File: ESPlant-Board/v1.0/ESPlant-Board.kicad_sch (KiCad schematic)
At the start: 24 parts, among them J2 Programmer, Q1 NPN, Q2 NPN, U1 ESP-12F

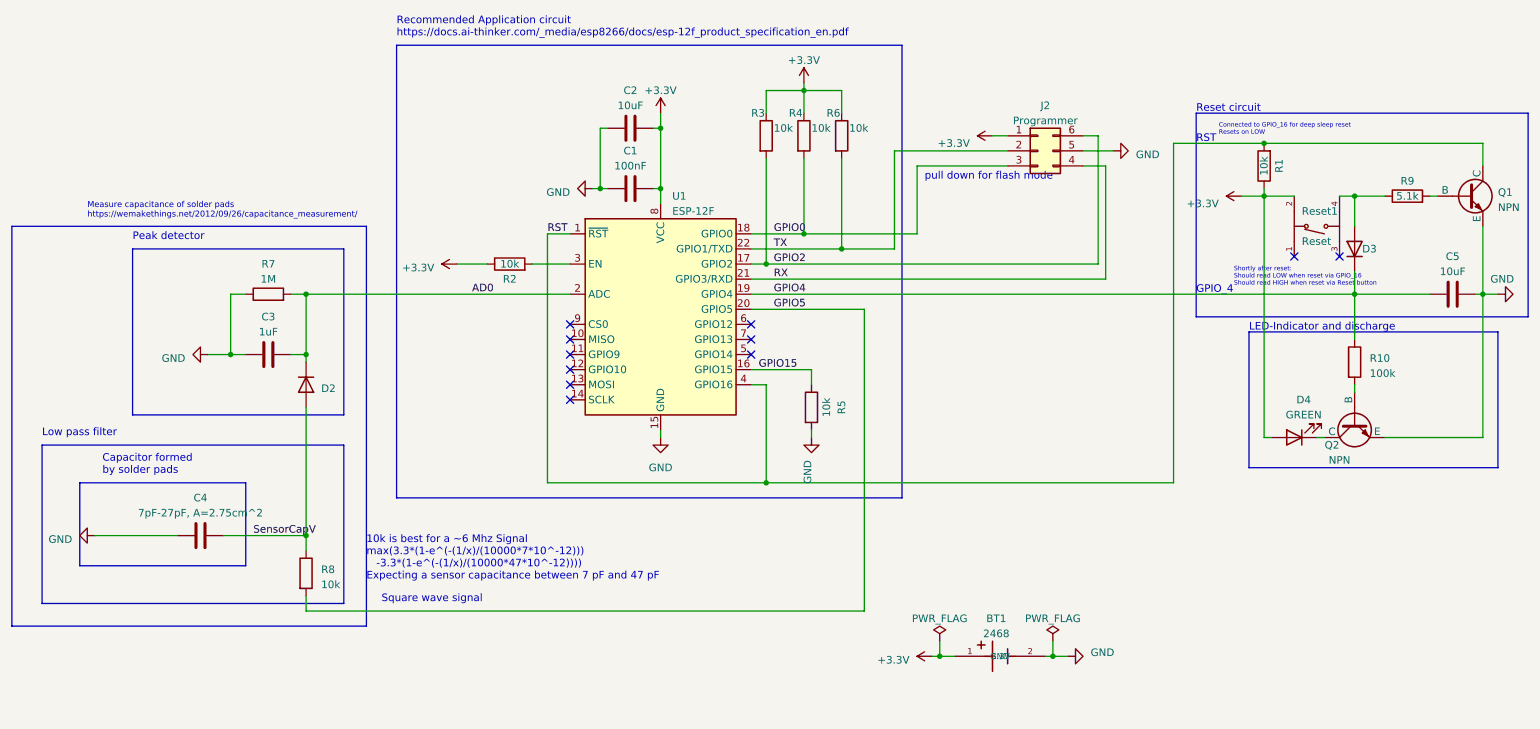
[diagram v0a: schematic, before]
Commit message: Replace layout to use battery pack
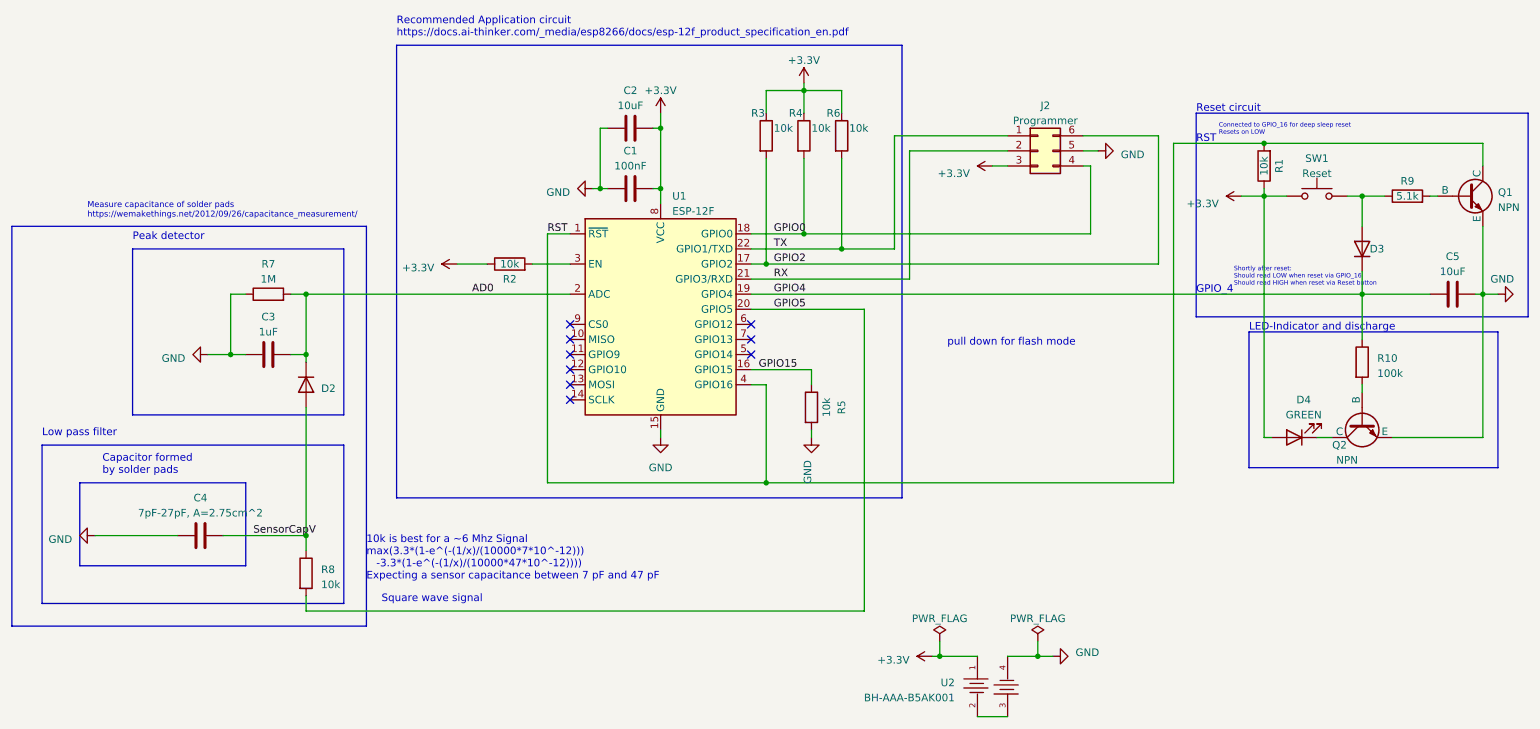
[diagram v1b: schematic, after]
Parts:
- removed BT1: 2468, CustomFootprints:BAT_2468, symbol Custom_Parts:2468
- removed Reset1: Reset, CustomFootprints:SW_Push_1P1T_XKB_TS-1187A, symbol Custom_Parts:TS-1187A-B-A-B
- added SW1: Reset, CustomFootprints:SW_Push_1P1T_XKB_TS-1187A, symbol Switch:SW_Push
- added U2: BH-AAA-B5AK001, CustomFootprints:BAT-SMD_BH-AAA-B5AA001, symbol Custom_Parts:BH-AAA-B5AK001
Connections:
- net +3.3V: now also J2.3 (Pin_3), SW1.1, U2.1 (+); no longer J2.1 (Pin_1)
- net GND: now also U2.4 (-)
- net GPIO0: now also J2.4 (Pin_4); no longer J2.3 (Pin_3)
- net RX: now also J2.2 (Pin_2); no longer J2.4 (Pin_4)
- net TX: now also J2.1 (Pin_1); no longer J2.2 (Pin_2)
- net at D3.2 (A), R9.1: now also SW1.2
- new net: U2.2 (-), U2.3 (+)
- no-connect marks 11 -> 9
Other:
- moved on the sheet: D3, Q2, R10
